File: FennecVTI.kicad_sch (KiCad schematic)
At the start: 56 parts, among them J1 Expansion Connector, J2 Slot Select, J3 Conn_Coaxial, J4 MDA/CGA connector, J5 DB15_Female, J6 DIP14 Keyboard Connector, J7 User Connector, Q1 2N3906, U1 74LS191, U10 74LS574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

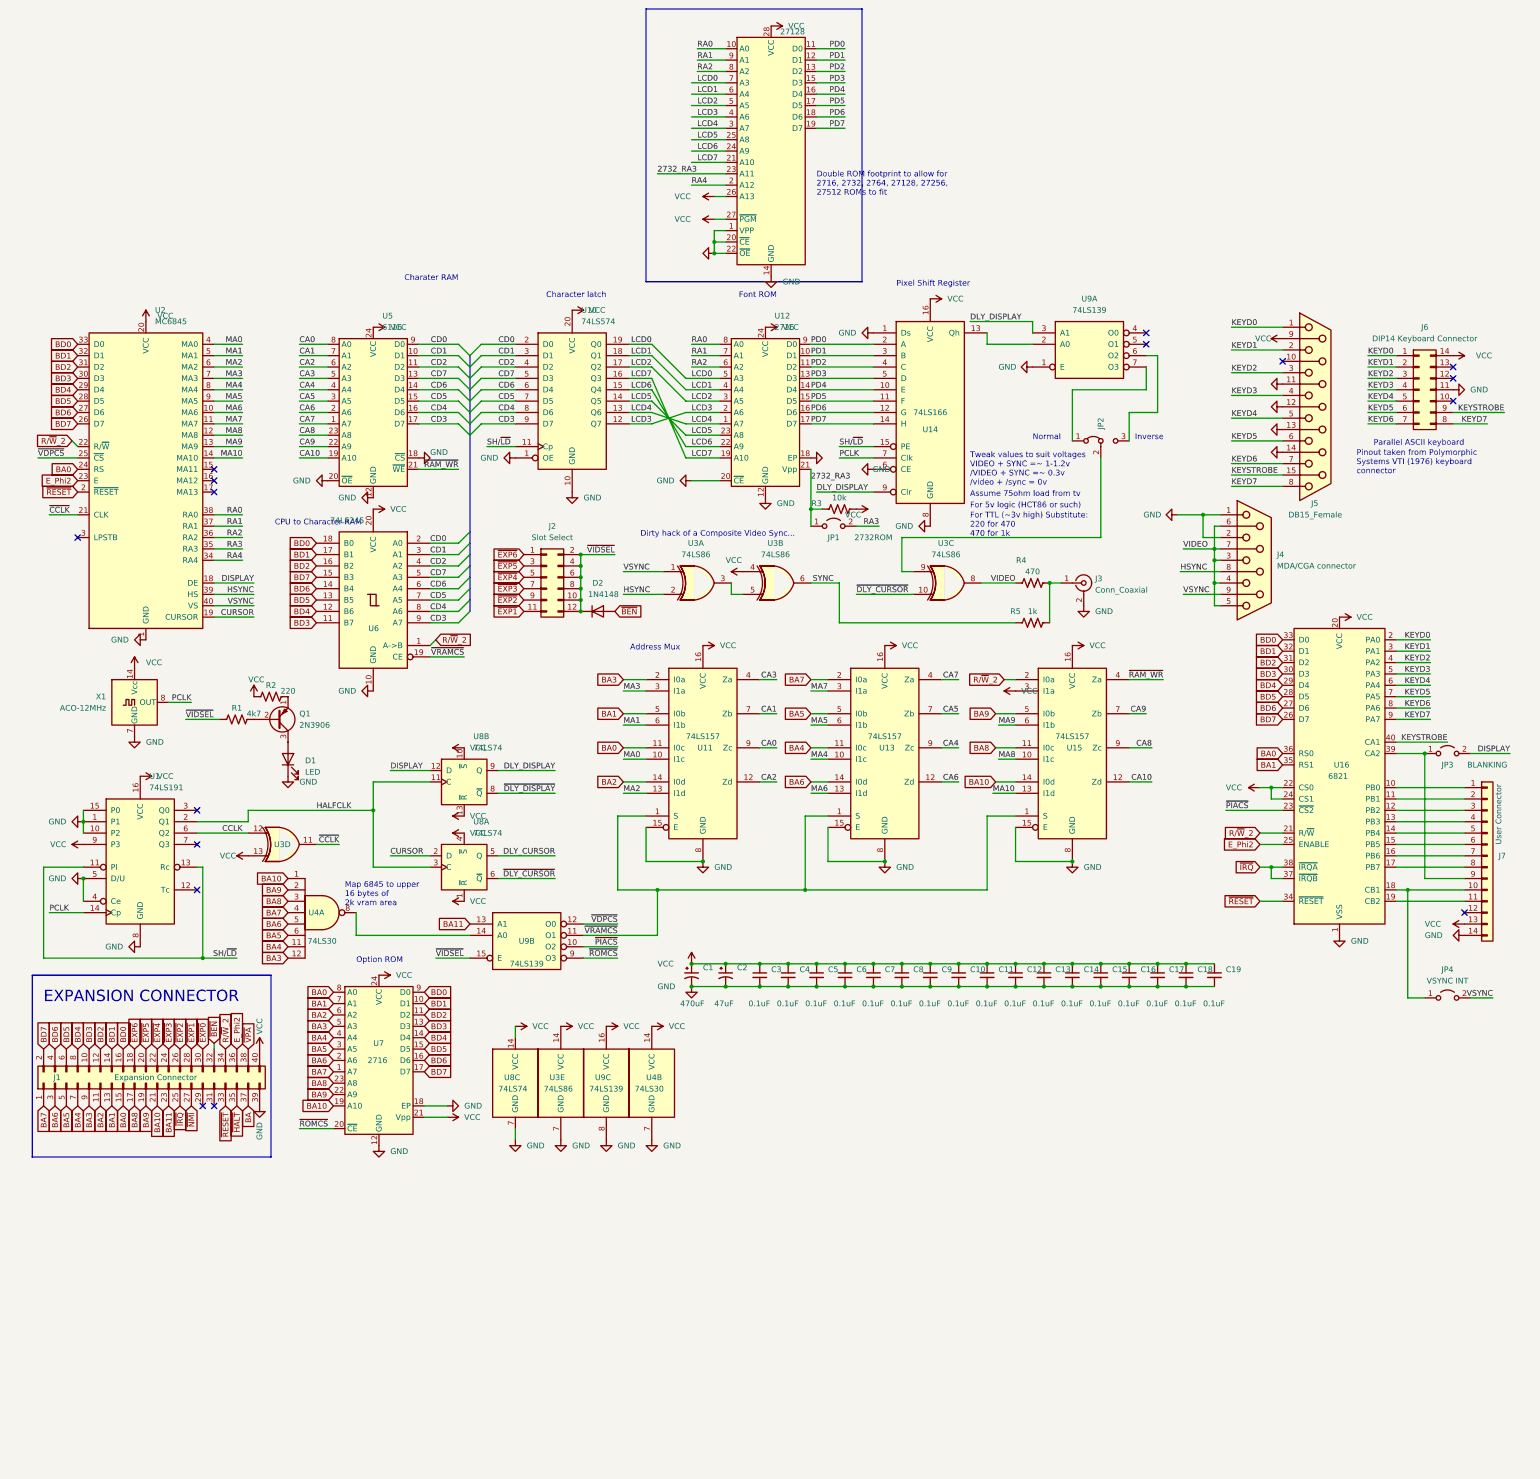
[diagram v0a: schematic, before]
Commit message: Added 2764 optional footprint for main rom. Rotated keyboard connector
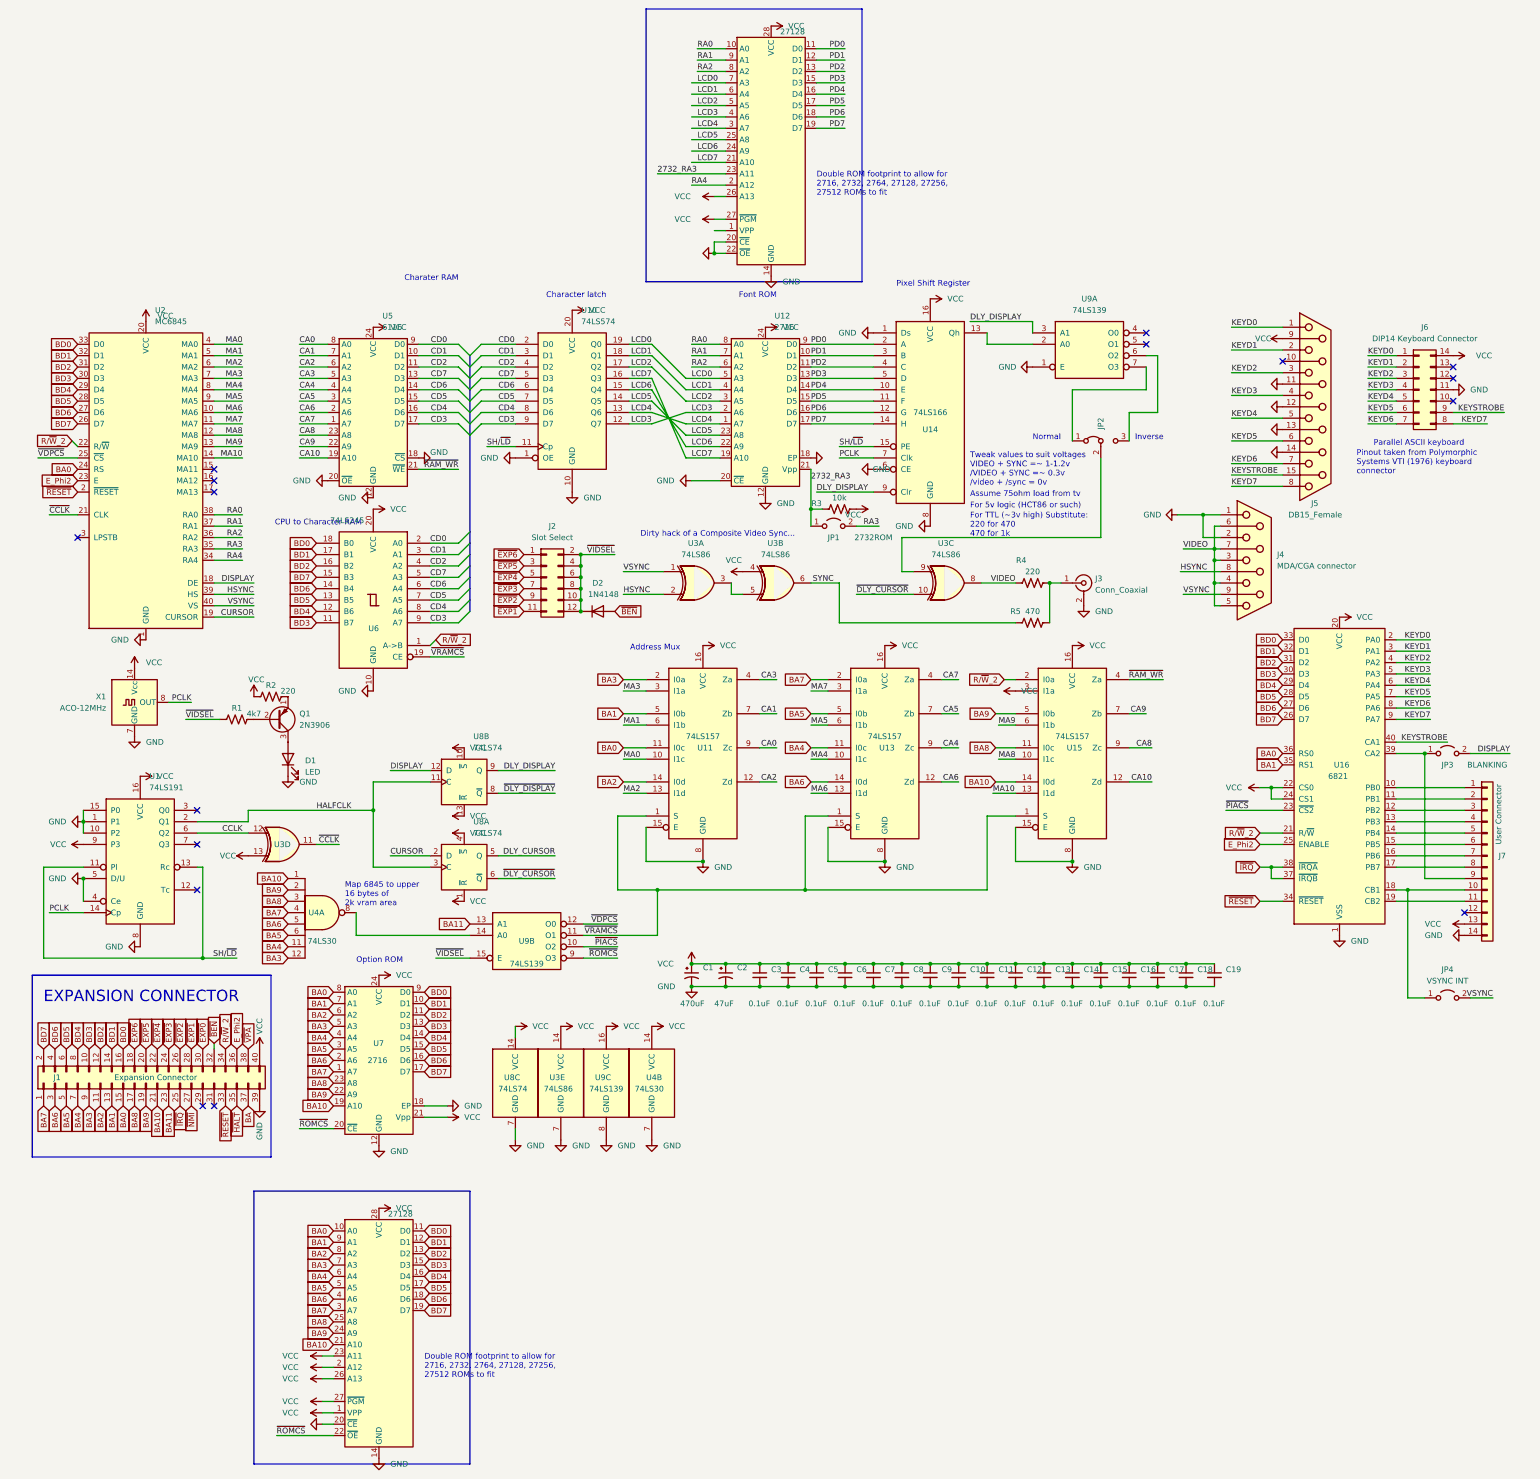
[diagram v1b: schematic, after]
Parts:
- added U70: 27128, Package_DIP:DIP-28_W15.24mm_Socket_LongPads, symbol Memory_EPROM:27128
- R4: value 470 -> 220
- R5: value 1k -> 470
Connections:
- net BA0: now also U70.10 (A0)
- net BA1: now also U70.9 (A1)
- net BA10: now also U70.21 (A10)
- net BA2: now also U70.8 (A2)
- net BA3: now also U70.7 (A3)
- net BA4: now also U70.6 (A4)
- net BA5: now also U70.5 (A5)
- net BA6: now also U70.4 (A6)
- net BA7: now also U70.3 (A7)
- net BA8: now also U70.25 (A8)
- net BA9: now also U70.24 (A9)
- net BD0: now also U70.11 (D0)
- net BD1: now also U70.12 (D1)
- net BD2: now also U70.13 (D2)
- net BD3: now also U70.15 (D3)
- net BD4: now also U70.16 (D4)
- net BD5: now also U70.17 (D5)
- net BD6: now also U70.18 (D6)
- net BD7: now also U70.19 (D7)
- net GND: now also U70.14 (GND), U70.20 (~{CE}); no longer U120.1 (VPP)
- net VCC: now also U70.1 (VPP), U70.2 (A12), U70.23 (A11), U70.26 (A13), U70.27 (~{PGM}), U70.28 (VCC)
- net ~{ROMCS}: now also U70.22 (~{OE})

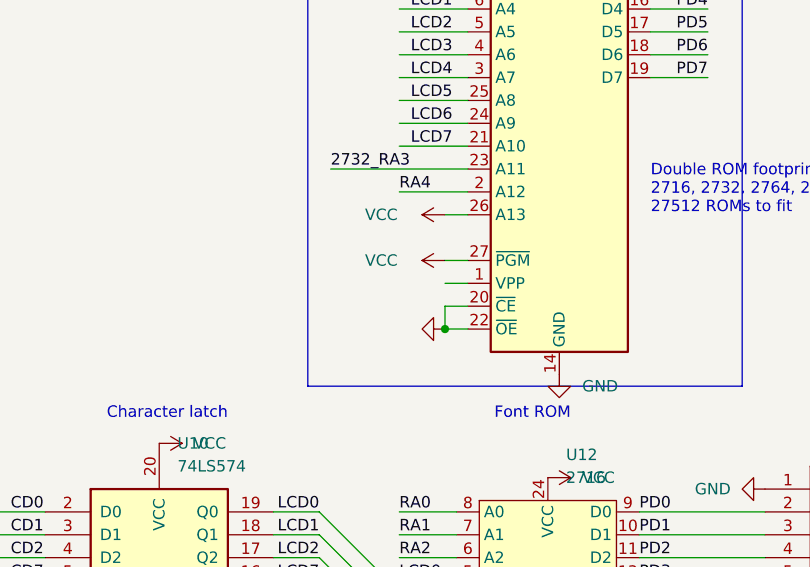
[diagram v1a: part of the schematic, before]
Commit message: Tweaked 2764 pinouts, cleanup DRC
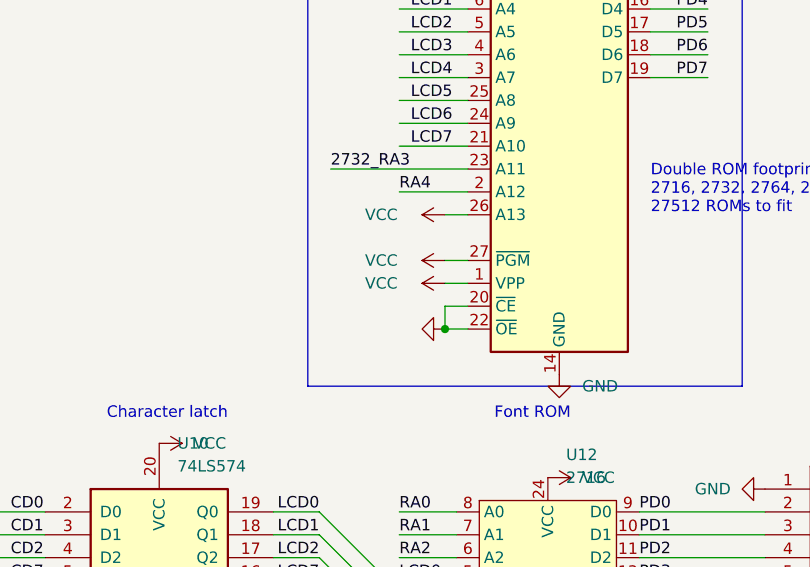
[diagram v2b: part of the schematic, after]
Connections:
- net VCC: now also U120.1 (VPP)
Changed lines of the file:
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@@
+    )
+  )
+  (symbol (lib_id "power:VCC") (at 165.1 -3.81 90) (unit 1)
+    (in_bom yes) (on_board yes) (dnp no)
+    (property "Reference" "#PWR087" (at 168.91 -3.81 0)
+      (effects (font (size 1.27 1.27)) hide)
+    )
+    (property "Value" "VCC" (at 156.21 -3.81 90)
+      (effects (font (size 1.27 1.27)) (justify right))
+    )
+    (property "Footprint" "" (at 165.1 -3.81 0)
+      (effects (font (size 1.27 1.27)) hide)
+    )
+    (property "Datasheet" "" (at 165.1 -3.81 0)
+      (effects (font (size 1.27 1.27)) hide)
+    )
+    (pin "1")
+    (instances
+      (project "FennecVTI"
+        (path "/07f4ff84-bbcc-43a3-8988-f6a9fc4547d7"
+          (reference "#PWR087") (unit 1)
+        )
+      )
     )
   )

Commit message: Updated ploted schmeatic
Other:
- moved on the sheet: C1, C10, C11, C12, C13, C14, C15, C16, C17, C18, C19, C2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
